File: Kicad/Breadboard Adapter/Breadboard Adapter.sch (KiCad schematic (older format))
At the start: 6 parts, among them J1 Bus_ISA_8bit, J2 USB_C_Receptacle_USB2.0, J3 Conn_01x31, J4 Conn_01x31, J9 Bus_ISA_8bit, SW1 SW_Push_DPDT

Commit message: update
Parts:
- added J5: Bus_ISA_8bit, My:8-bit-ISA, symbol Connector:Bus_ISA_8bit
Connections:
- net 12+: now also J5.9 (+12V)
- net 12-: now also J5.7 (-12V)
- net 5+: now also J5.29 (VCC), J5.3 (VCC)
- net 5-: now also J5.5 (-5V)
- net A0: now also J5.62 (BA00)
- net A1: now also J5.61 (BA01)
- net A10: now also J5.52 (BA10)
- net A11: now also J5.51 (BA11)
- net A12: now also J5.50 (BA12)
- net A13: now also J5.49 (BA13)
- net A14: now also J5.48 (BA14)
- net A15: now also J5.47 (BA15)
- net A16: now also J5.46 (BA16)
- net A17: now also J5.45 (BA17)
- net A18: now also J5.44 (BA18)
- net A19: now also J5.43 (BA19)
- net A2: now also J5.60 (BA02)
- net A3: now also J5.59 (BA03)
- net A4: now also J5.58 (BA04)
- net A5: now also J5.57 (BA05)
- net A6: now also J5.56 (BA06)
- net A7: now also J5.55 (BA07)
- net A8: now also J5.54 (BA08)
- net A9: now also J5.53 (BA09)
- net AEN: now also J5.42 (AEN)
- net ALE: now also J5.28 (ALE)
- net CH_CK: now also J5.32 (IO)
- net CLK88: now also J5.20 (CLK)
- net D0: now also J5.40 (DB0)
- net D1: now also J5.39 (DB1)
- net D2: now also J5.38 (DB2)
- net D3: now also J5.37 (DB3)
- net D4: now also J5.36 (DB4)
- net D5: now also J5.35 (DB5)
- net D6: now also J5.34 (DB6)
- net D7: now also J5.33 (DB7)
- net DACK1: now also J5.17 (~DACK1)
- net DACK2: now also J5.26 (~DACK2)
- net DACK3: now also J5.15 (~DACK3)
- net DRQ1: now also J5.18 (DRQ1)
- net DRQ2: now also J5.6 (DRQ2)
- net DRQ3: now also J5.16 (DRQ3)
- net GND: now also J5.1 (GND), J5.10 (GND), J5.31 (GND)
- net IORD: now also J5.14 (~IOR)
- net IOWR: now also J5.13 (~IOW)
- net IRQ2: now also J5.4 (IRQ2)
- net IRQ3: now also J5.25 (IRQ3)
- net IRQ4: now also J5.24 (IRQ4)
- net IRQ5: now also J5.23 (IRQ5)
- net IRQ6: now also J5.22 (IRQ6)
- net IRQ7: now also J5.21 (IRQ7)
- net MRD: now also J5.12 (~SMEMR)
- net MWR: now also J5.11 (~SMEMW)
- net NC: now also J5.8 (UNUSED)
- net OSC88: now also J5.30 (OSC)
- net RDY1: now also J5.41 (IO_READY)
- net REFRQ: now also J5.19 (~DACK0)
- net RESOUT: now also J5.2 (RESET)
- net TC: now also J5.27 (TC)
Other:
- moved on the sheet: J4
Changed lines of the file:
@@
 L Connector_Generic:Conn_01x31 J4
 U 1 1 636509A5
-P 14850 4950
-F 0 "J4" H 14768 6667 50  0000 C CNN
-F 1 "Conn_01x31" H 14768 6576 50  0000 C CNN
-F 2 "Connector_PinHeader_2.54mm:PinHeader_1x31_P2.54mm_Vertical" H 14850 4950 50  0001 C CNN
-F 3 "~" H 14850 4950 50  0001 C CNN
-	1    14850 4950
+P 17250 5000
+F 0 "J4" H 17168 6717 50  0000 C CNN
+F 1 "Conn_01x31" H 17168 6626 50  0000 C CNN
+F 2 "Connector_PinHeader_2.54mm:PinHeader_1x31_P2.54mm_Vertical" H 17250 5000 50  0001 C CNN
+F 3 "~" H 17250 5000 50  0001 C CNN
+	1    17250 5000
 	-1   0    0    -1
 $EndComp
@@
 Text Label 8400 4775 2    50   ~ 0
 IORD
-Text Label 15050 3550 0    50   ~ 0
+Text Label 17450 3600 0    50   ~ 0
 D7
-Text Label 15050 3650 0    50   ~ 0
+Text Label 17450 3700 0    50   ~ 0
 D6
-Text Label 15050 3750 0    50   ~ 0
+Text Label 17450 3800 0    50   ~ 0
 D5
-Text Label 15050 3850 0    50   ~ 0
+Text Label 17450 3900 0    50   ~ 0
 D4
-Text Label 15050 3950 0    50   ~ 0
+Text Label 17450 4000 0    50   ~ 0
 D3
-Text Label 15050 4050 0    50   ~ 0
+Text Label 17450 4100 0    50   ~ 0
 D2
-Text Label 15050 4150 0    50   ~ 0
+Text Label 17450 4200 0    50   ~ 0
 D1
-Text Label 15050 4250 0    50   ~ 0
+Text Label 17450 4300 0    50   ~ 0
 D0
-Text Label 15050 4350 0    50   ~ 0
+Text Label 17450 4400 0    50   ~ 0
 RDY1
-Text Label 15050 4450 0    50   ~ 0
+Text Label 17450 4500 0    50   ~ 0
 AEN
-Text Label 15050 4550 0    50   ~ 0
+Text Label 17450 4600 0    50   ~ 0
 A19
-Text Label 15050 4650 0    50   ~ 0
+Text Label 17450 4700 0    50   ~ 0
 A18
-Text Label 15050 4750 0    50   ~ 0
+Text Label 17450 4800 0    50   ~ 0
 A17
-Text Label 15050 4850 0    50   ~ 0
+Text Label 17450 4900 0    50   ~ 0
 A16
-Text Label 15050 4950 0    50   ~ 0
+Text Label 17450 5000 0    50   ~ 0
 A15
-Text Label 15050 5050 0    50   ~ 0
+Text Label 17450 5100 0    50   ~ 0
 A14
-Text Label 15050 5150 0    50   ~ 0
+Text Label 17450 5200 0    50   ~ 0
 A13
-Text Label 15050 5250 0    50   ~ 0
+Text Label 17450 5300 0    50   ~ 0
 A12
-Text Label 15050 5350 0    50   ~ 0
+Text Label 17450 5400 0    50   ~ 0
 A11
-Text Label 15050 5450 0    50   ~ 0
+Text Label 17450 5500 0    50   ~ 0
 A10
-Text Label 15050 5550 0    50   ~ 0
+Text Label 17450 5600 0    50   ~ 0
 A9
-Text Label 15050 5650 0    50   ~ 0
+Text Label 17450 5700 0    50   ~ 0
 A8
-Text Label 15050 5750 0    50   ~ 0
+Text Label 17450 5800 0    50   ~ 0
 A7
-Text Label 15050 5850 0    50   ~ 0
+Text Label 17450 5900 0    50   ~ 0
 A6
-Text Label 15050 5950 0    50   ~ 0
+Text Label 17450 6000 0    50   ~ 0
 A5
-Text Label 15050 6050 0    50   ~ 0
+Text Label 17450 6100 0    50   ~ 0
 A4
-Text Label 15050 6150 0    50   ~ 0
+Text Label 17450 6200 0    50   ~ 0
 A3
-Text Label 15050 6250 0    50   ~ 0
+Text Label 17450 6300 0    50   ~ 0
 A2
-Text Label 15050 6350 0    50   ~ 0
+Text Label 17450 6400 0    50   ~ 0
 A1
-Text Label 15050 3450 0    50   ~ 0
+Text Label 17450 3500 0    50   ~ 0
 CH_CK
-Text Label 15050 6450 0    50   ~ 0
+Text Label 17450 6500 0    50   ~ 0
 A0
 Text Label 12075 4300 2    50   ~ 0
@@
 Text Label 13475 3600 0    50   ~ 0
 D7
+Text Label 14700 4225 2    50   ~ 0
+12+
+Text Label 14700 4025 2    50   ~ 0
+12-
+Text Label 14700 3925 2    50   ~ 0
+DRQ2
+Text Label 14700 3825 2    50   ~ 0
+5-
+Text Label 14700 3725 2    50   ~ 0
+IRQ2
+Text Label 14700 3625 2    50   ~ 0
+5+
+Text Label 14700 3525 2    50   ~ 0
+RESOUT
+Text Label 14700 3425 2    50   ~ 0
+GND
+Text Label 14700 4825 2    50   ~ 0
+DACK3
+Text Label 14700 4925 2    50   ~ 0
+DRQ3
+Text Label 14700 5025 2    50   ~ 0
+DACK1
+Text Label 14700 5125 2    50   ~ 0
+DRQ1
+Text Label 14700 5225 2    50   ~ 0
+REFRQ
+Text Label 14700 5325 2    50   ~ 0
+CLK88
+Text Label 14700 5425 2    50   ~ 0
+IRQ7
+Text Label 14700 5525 2    50   ~ 0
+IRQ6
+Text Label 14700 5625 2    50   ~ 0
+IRQ5
+Text Label 14700 5725 2    50   ~ 0
+IRQ4
+Text Label 14700 5825 2    50   ~ 0
+IRQ3
+Text Label 14700 5925 2    50   ~ 0
+DACK2
+Text Label 14700 6025 2    50   ~ 0
+TC
+Text Label 14700 6125 2    50   ~ 0
+ALE
+Text Label 14700 6225 2    50   ~ 0
+5+
+Text Label 14700 4125 2    50   ~ 0
+NC
+Text Label 14700 6325 2    50   ~ 0
+OSC88
+Text Label 14700 6425 2    50   ~ 0
+GND
+Text Label 14700 4325 2    50   ~ 0
+GND
+Text Label 14700 4425 2    50   ~ 0
+MWR
+Text Label 14700 4525 2    50   ~ 0
+MRD
+Text Label 14700 4625 2    50   ~ 0
+IOWR
+Text Label 14700 4725 2    50   ~ 0
+IORD
+$Comp
+L Connector:Bus_ISA_8bit J5
+U 1 1 66563874
+P 15400 4925
+F 0 "J5" H 15400 6692 50  0001 C CNN
+F 1 "Bus_ISA_8bit" H 15400 6601 50  0001 C CNN
+F 2 "My:8-bit-ISA" H 15400 4925 50  0001 C CNN
+F 3 "https://en.wikipedia.org/wiki/Industry_Standard_Architecture" H 15400 4925 50  0001 C CNN
+	1    15400 4925
+	1    0    0    -1
+$EndComp
+Text Label 16100 6425 0    50   ~ 0
+A0
+Text Label 16100 3425 0    50   ~ 0
+CH_CK
+Text Label 16100 6325 0    50   ~ 0
+A1
+Text Label 16100 6225 0    50   ~ 0
+A2
+Text Label 16100 6125 0    50   ~ 0
+A3
+Text Label 16100 6025 0    50   ~ 0
+A4
+Text Label 16100 5925 0    50   ~ 0
+A5
+Text Label 16100 5825 0    50   ~ 0
+A6
+Text Label 16100 5725 0    50   ~ 0
+A7
+Text Label 16100 5625 0    50   ~ 0
+A8
+Text Label 16100 5525 0    50   ~ 0
+A9
+Text Label 16100 5425 0    50   ~ 0
+A10
+Text Label 16100 5325 0    50   ~ 0
+A11
+Text Label 16100 5225 0    50   ~ 0
+A12
+Text Label 16100 5125 0    50   ~ 0
+A13
+Text Label 16100 5025 0    50   ~ 0
+A14
+Text Label 16100 4925 0    50   ~ 0
+A15
+Text Label 16100 4825 0    50   ~ 0
+A16
+Text Label 16100 4725 0    50   ~ 0
+A17
+Text Label 16100 4625 0    50   ~ 0
+A18
+Text Label 16100 4525 0    50   ~ 0
+A19
+Text Label 16100 4425 0    50   ~ 0
+AEN
+Text Label 16100 4325 0    50   ~ 0
+RDY1
+Text Label 16100 4225 0    50   ~ 0
+D0
+Text Label 16100 4125 0    50   ~ 0
+D1
+Text Label 16100 4025 0    50   ~ 0
+D2
+Text Label 16100 3925 0    50   ~ 0
+D3
+Text Label 16100 3825 0    50   ~ 0
+D4
+Text Label 16100 3725 0    50   ~ 0
+D5
+Text Label 16100 3625 0    50   ~ 0
+D6
+Text Label 16100 3525 0    50   ~ 0
+D7
 $EndSCHEMATC

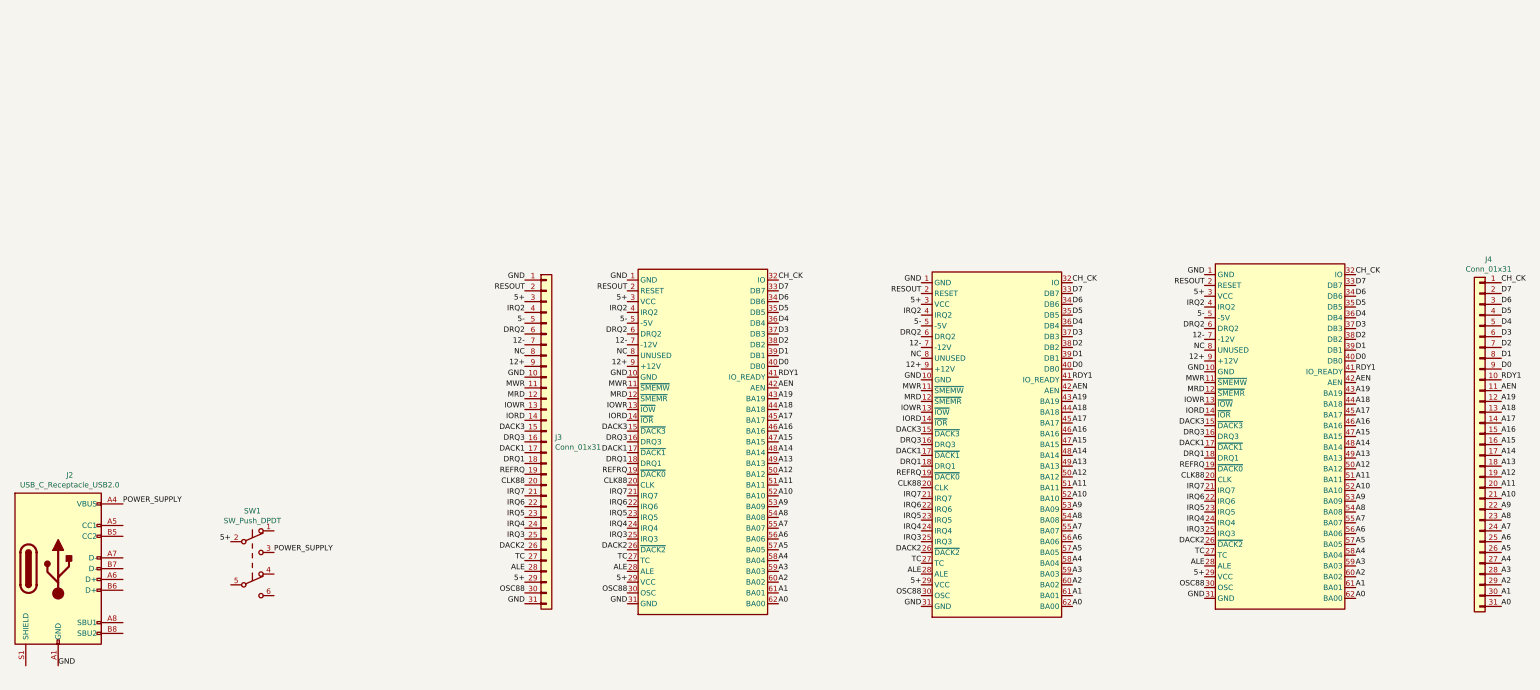
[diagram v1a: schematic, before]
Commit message: Up dated Breadboard adpater
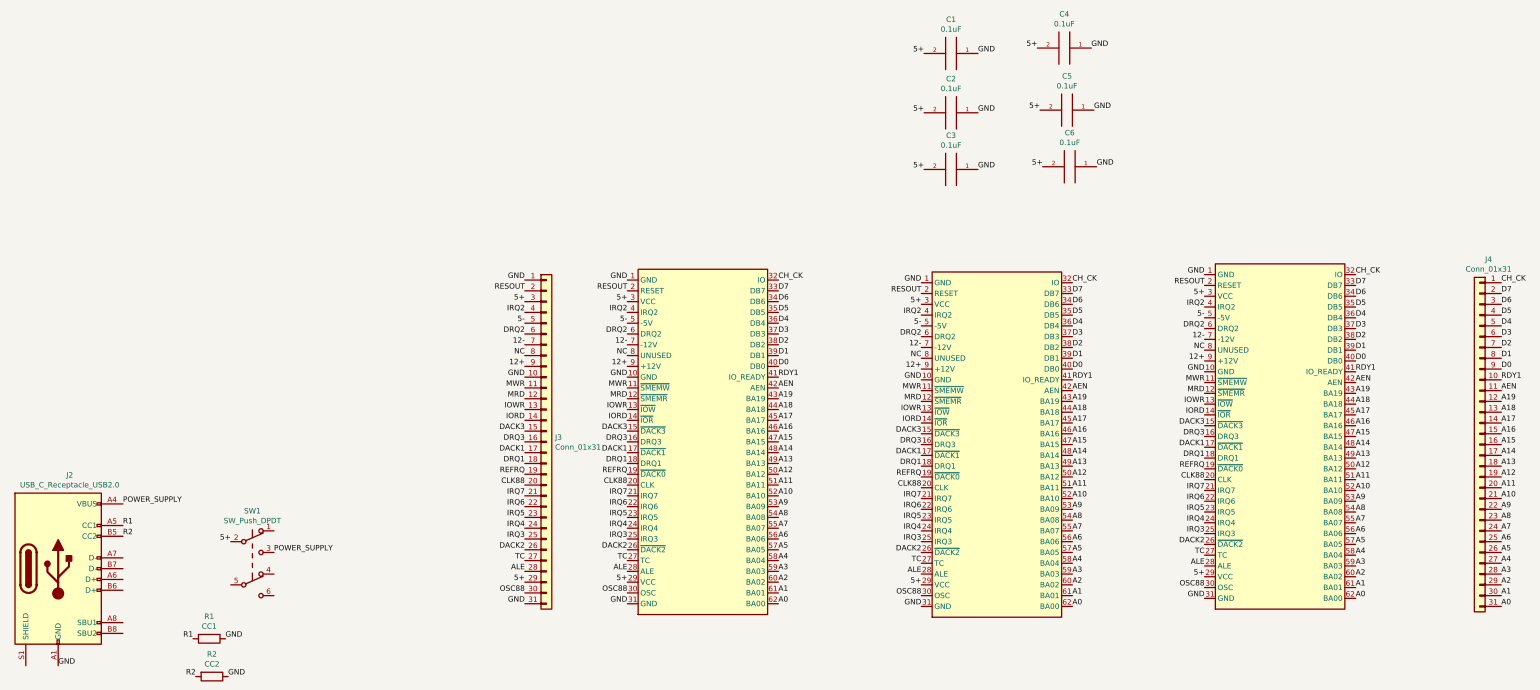
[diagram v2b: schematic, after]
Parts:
- added C1, C2, C3, C4, C5, C6: 0.1uF, Capacitor_THT:C_Disc_D4.3mm_W1.9mm_P5.00mm, symbol pspice:CAP
- added R1: CC1, Resistor_THT:R_Axial_DIN0207_L6.3mm_D2.5mm_P10.16mm_Horizontal, symbol Device:R
- added R2: CC2, Resistor_THT:R_Axial_DIN0207_L6.3mm_D2.5mm_P10.16mm_Horizontal, symbol Device:R
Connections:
- net 5+: now also C1.2, C2.2, C3.2, C4.2, C5.2, C6.2
- net GND: now also C1.1, C2.1, C3.1, C4.1, C5.1, C6.1, R1.1, R2.1
- net R1: now reaches J2.A5 (CC1)
- net R1: now also R1.2
- net R2: now reaches J2.B5 (CC2)
- net R2: now also R2.2
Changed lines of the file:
@@
 Text Label 16100 3525 0    50   ~ 0
 D7
+$Comp
+L Device:R R1
+U 1 1 679BF871
+P 5475 6800
+F 0 "R1" V 5268 6800 50  0000 C CNN
+F 1 "CC1" V 5359 6800 50  0000 C CNN
+F 2 "Resistor_THT:R_Axial_DIN0207_L6.3mm_D2.5mm_P10.16mm_Horizontal" V 5405 6800 50  0001 C CNN
+F 3 "~" H 5475 6800 50  0001 C CNN
+	1    5475 6800
+	0    1    1    0
+$EndComp
+Text Label 4675 5750 0    50   ~ 0
+R1
+Text Label 4675 5850 0    50   ~ 0
+R2
+Text Label 5625 6800 0    50   ~ 0
+GND
+$Comp
+L Device:R R2
+U 1 1 679C0E22
+P 5500 7150
+F 0 "R2" V 5293 7150 50  0000 C CNN
+F 1 "CC2" V 5384 7150 50  0000 C CNN
+F 2 "Resistor_THT:R_Axial_DIN0207_L6.3mm_D2.5mm_P10.16mm_Horizontal" V 5430 7150 50  0001 C CNN
+F 3 "~" H 5500 7150 50  0001 C CNN
+	1    5500 7150
+	0    1    1    0
+$EndComp
+Text Label 5650 7150 0    50   ~ 0
+GND
+Text Label 5325 6800 2    50   ~ 0
+R1
+Text Label 5350 7150 2    50   ~ 0
+R2
+$Comp
+L pspice:CAP C1
+U 1 1 679D483C
+P 12350 1375
+F 0 "C1" V 12035 1375 50  0000 C CNN
+F 1 "0.1uF" V 12126 1375 50  0000 C CNN
+F 2 "Capacitor_THT:C_Disc_D4.3mm_W1.9mm_P5.00mm" H 12350 1375 50  0001 C CNN
+F 3 "~" H 12350 1375 50  0001 C CNN
+	1    12350 1375
+	0    1    1    0
+$EndComp
+Text Label 12100 1375 2    50   ~ 0
+5+
+Text Label 12600 1375 0    50   ~ 0
+GND
+$Comp
+L pspice:CAP C2
+U 1 1 679D638C
+P 12350 1925
+F 0 "C2" V 12035 1925 50  0000 C CNN
+F 1 "0.1uF" V 12126 1925 50  0000 C CNN
+F 2 "Capacitor_THT:C_Disc_D4.3mm_W1.9mm_P5.00mm" H 12350 1925 50  0001 C CNN
+F 3 "~" H 12350 1925 50  0001 C CNN
+	1    12350 1925
+	0    1    1    0
+$EndComp
+Text Label 12100 1925 2    50   ~ 0
+5+
+Text Label 12600 1925 0    50   ~ 0
+GND
+$Comp
+L pspice:CAP C3
+U 1 1 679D674E
+P 12350 2450
+F 0 "C3" V 12035 2450 50  0000 C CNN
+F 1 "0.1uF" V 12126 2450 50  0000 C CNN
+F 2 "Capacitor_THT:C_Disc_D4.3mm_W1.9mm_P5.00mm" H 12350 2450 50  0001 C CNN
+F 3 "~" H 12350 2450 50  0001 C CNN
+	1    12350 2450
+	0    1    1    0
+$EndComp
+Text Label 12100 2450 2    50   ~ 0
+5+
+Text Label 12600 2450 0    50   ~ 0
+GND
+$Comp
+L pspice:CAP C4
+U 1 1 679D698C
+P 13400 1325
+F 0 "C4" V 13085 1325 50  0000 C CNN
+F 1 "0.1uF" V 13176 1325 50  0000 C CNN
+F 2 "Capacitor_THT:C_Disc_D4.3mm_W1.9mm_P5.00mm" H 13400 1325 50  0001 C CNN
+F 3 "~" H 13400 1325 50  0001 C CNN
+	1    13400 1325
+	0    1    1    0
+$EndComp
+Text Label 13150 1325 2    50   ~ 0
+5+
+Text Label 13650 1325 0    50   ~ 0
+GND
+$Comp
+L pspice:CAP C5
+U 1 1 679E0495
+P 13425 1900
+F 0 "C5" V 13110 1900 50  0000 C CNN
+F 1 "0.1uF" V 13201 1900 50  0000 C CNN
+F 2 "Capacitor_THT:C_Disc_D4.3mm_W1.9mm_P5.00mm" H 13425 1900 50  0001 C CNN
+F 3 "~" H 13425 1900 50  0001 C CNN
+	1    13425 1900
+	0    1    1    0
+$EndComp
+Text Label 13175 1900 2    50   ~ 0
+5+
+Text Label 13675 1900 0    50   ~ 0
+GND
+$Comp
+L pspice:CAP C6
+U 1 1 679E0A2B
+P 13450 2425
+F 0 "C6" V 13135 2425 50  0000 C CNN
+F 1 "0.1uF" V 13226 2425 50  0000 C CNN
+F 2 "Capacitor_THT:C_Disc_D4.3mm_W1.9mm_P5.00mm" H 13450 2425 50  0001 C CNN
+F 3 "~" H 13450 2425 50  0001 C CNN
+	1    13450 2425
+	0    1    1    0
+$EndComp
+Text Label 13200 2425 2    50   ~ 0
+5+
+Text Label 13700 2425 0    50   ~ 0
+GND
 $EndSCHEMATC
